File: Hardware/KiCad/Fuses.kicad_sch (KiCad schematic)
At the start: 7 parts, among them Q2 771-BUK6M61-60PX

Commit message: software pr
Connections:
- net FANS_IN: now also 12V1.2 (A), R_PD3.2
- net at Q2.4 (G), R_G3.1: no longer 12V1.2 (A), R_PD3.2
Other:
- moved on the sheet: R_G3
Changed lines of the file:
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@@
 	(wire
 		(pts
-			(xy 74.93 77.47) (xy 80.01 77.47)
+			(xy 74.93 77.47) (xy 91.44 77.47)
 		)
 		(stroke
@@
 	(wire
 		(pts
+			(xy 102.87 77.47) (xy 113.03 77.47)
+		)
+		(stroke
+			(width 0)
+			(type default)
+		)
+	)
+	(wire
+		(pts
 			(xy 102.87 59.69) (xy 102.87 64.77)
 		)
@@
 	(wire
 		(pts
-			(xy 87.63 77.47) (xy 91.44 77.47)
-		)
-		(stroke
-			(width 0)
-			(type default)
-		)
-	)
-	(wire
-		(pts
 			(xy 110.49 66.04) (xy 113.03 66.04)
 		)
@@
 	(wire
 		(pts
-			(xy 91.44 77.47) (xy 113.03 77.47)
+			(xy 91.44 77.47) (xy 95.25 77.47)
 		)
 		(stroke
@@
 	(symbol
 		(lib_id "Device:R")
-		(at 83.82 77.47 270)
+		(at 99.06 77.47 270)
 		(unit 1)
 		(exclude_from_sim no)
@@
 		(dnp no)
 		(property "Reference" "R_G3"
-			(at 81.788 75.184 90)
+			(at 97.028 75.184 90)
 			(effects
 				(font
@@
 		)
 		(property "Value" "100"
-			(at 81.788 80.01 90)
+			(at 97.028 80.01 90)
 			(effects
 				(font
@@
 		)
 		(property "Footprint" "Resistor_SMD:R_0603_1608Metric_Pad0.98x0.95mm_HandSolder"
-			(at 83.82 75.692 90)
+			(at 99.06 75.692 90)
 			(effects
 				(font
@@
 		)
 		(property "Datasheet" "~"
-			(at 83.82 77.47 0)
+			(at 99.06 77.47 0)
 			(effects
 				(font
@@
 		)
 		(property "Description" "Resistor"
-			(at 83.82 77.47 0)
+			(at 99.06 77.47 0)
 			(effects
 				(font
@@
 		)
 		(property "Manufacturer" ""
-			(at 83.82 77.47 90)
+			(at 99.06 77.47 90)
 			(effects
 				(font
@@
 		)
 		(property "Mouser Link" ""
-			(at 83.82 77.47 90)
+			(at 99.06 77.47 90)
 			(effects
 				(font
@@
 		)
 		(property "Manufacturer_Part_Number" "CRCW0603120RFKEC "
-			(at 83.82 77.47 90)
+			(at 99.06 77.47 90)
 			(effects
 				(font
@@
 		)
 		(property "Sim.Type" ""
-			(at 83.82 77.47 90)
+			(at 99.06 77.47 90)
 			(effects
 				(font
@@
 		)
 		(property "Description (Customer #)" ""
-			(at 83.82 77.47 90)
-			(effects
-				(font
+			(at 99.06 77.47 90)
+			(effects
+				(font

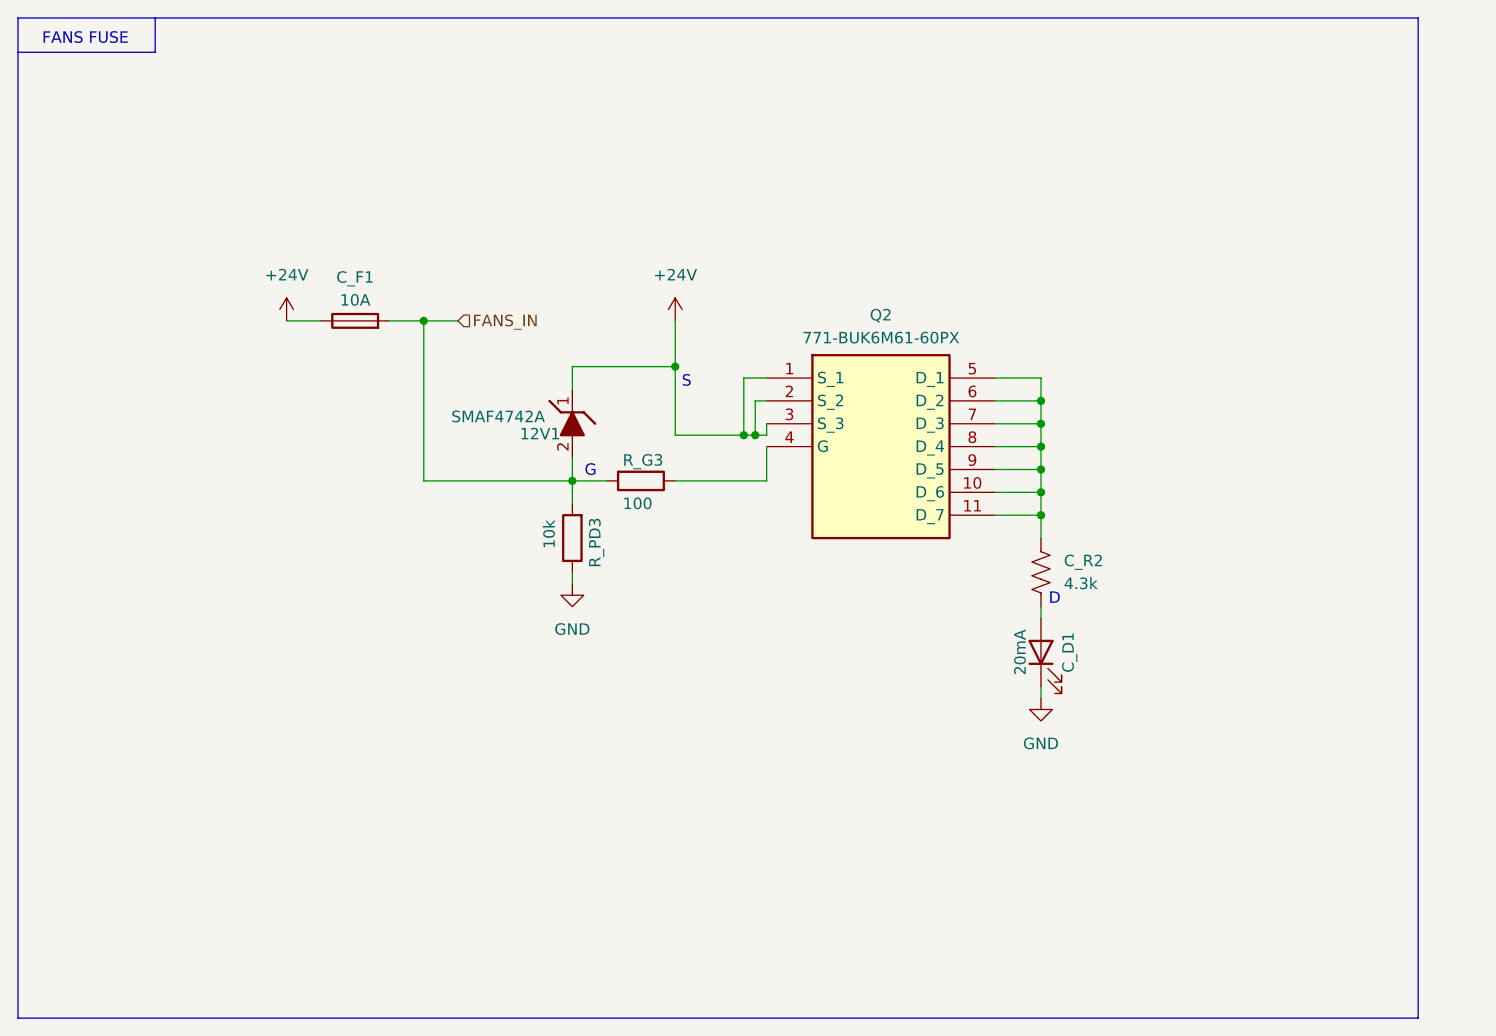
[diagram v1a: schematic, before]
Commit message: schematic changes, pre pcb revB changes
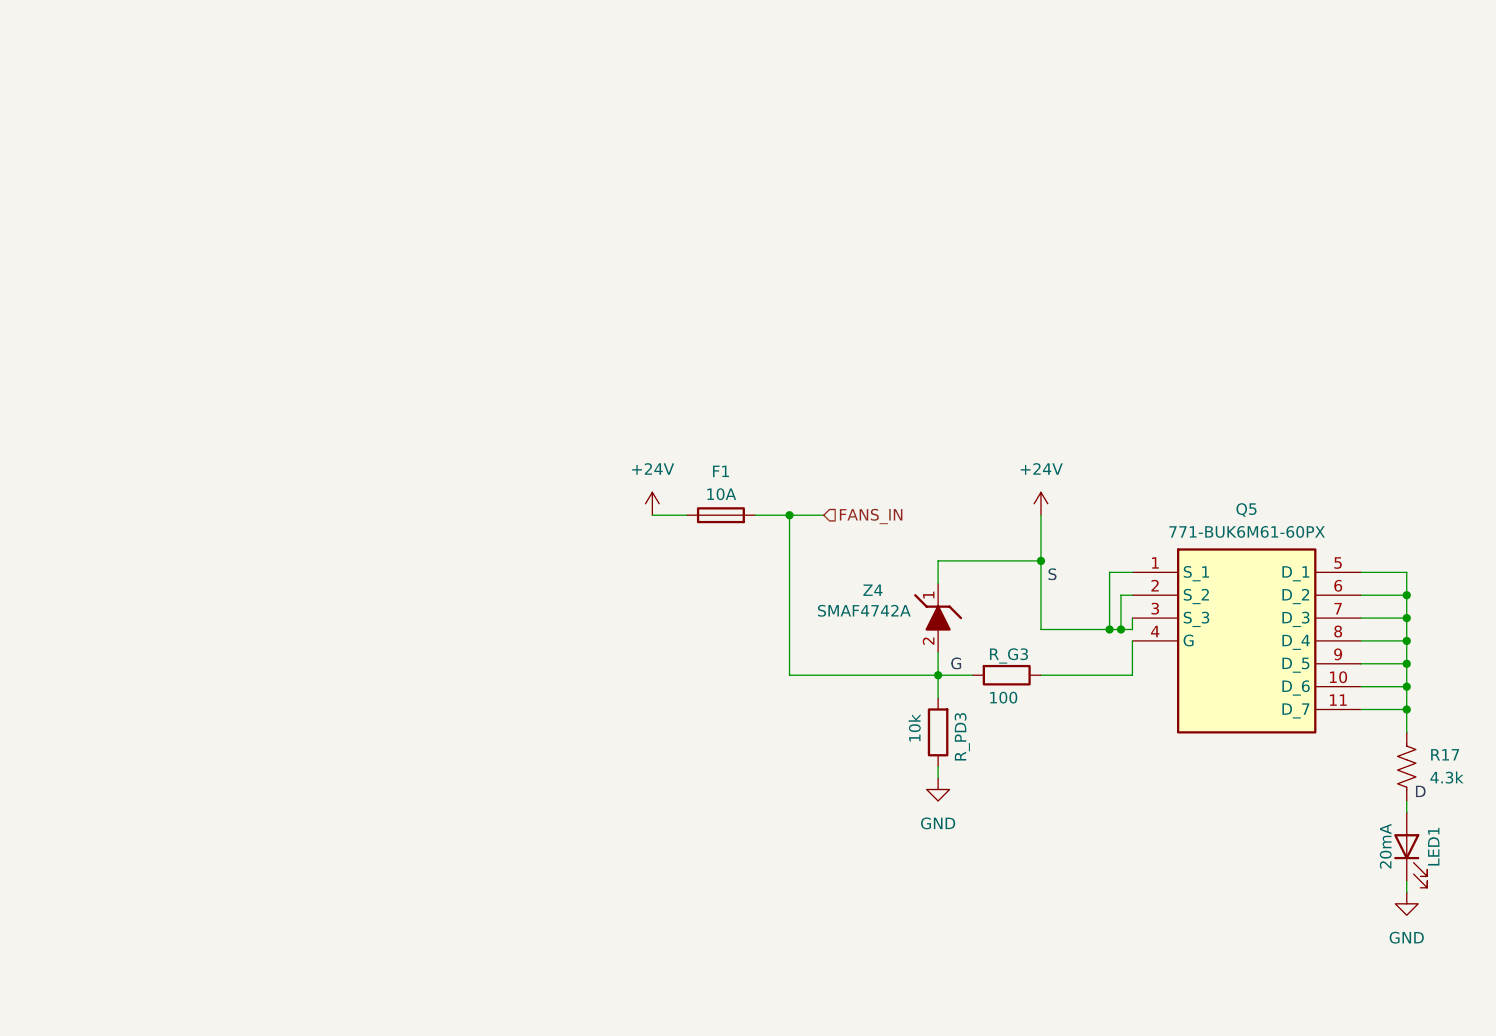
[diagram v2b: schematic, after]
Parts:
- F1: renamed from C_F1; footprint Fuse:FUSE_3568 -> Moco:FUSE_3568; LCSC (none) -> C5249699
- Q5: renamed from Q2; footprint UTSVT_Passives:BUK9M34100EX -> Moco:BUK9M34100EX
- R17: renamed from C_R2; footprint Resistor_SMD:R_0805_2012Metric -> Resistor_SMD:R_0805_2012Metric_Pad1.20x1.40mm_HandSolder
- R_PD3: LCSC (none) -> C25804
- Z4: renamed from 12V1; LCSC (none) -> C169537; Mouser Part Number 833-SMAF4749A-TP -> (none)
- renumbered C_D1 to LED1
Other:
- note removed: "FANS FUSE"
- moved on the sheet: F1, LED1, Q5, R17, R_G3, R_PD3, Z4

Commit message: sch changes, pre pcb changes
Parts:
- renumbered R17 to R15
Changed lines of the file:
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@@
 		(on_board yes)
 		(dnp no)
-		(property "Reference" "#PWR043"
+		(property "Reference" "#PWR041"
 			(at 143.51 85.09 0)
 			(effects
@@
 			(project "PS-MotorControllerInterfacePCB"
 				(path "/a2e13c19-ff3a-4e43-a7f5-200fd5b2b978/07f22498-fffc-46fc-8b11-2ac98c172822"
-					(reference "#PWR043")
+					(reference "#PWR041")
 					(unit 1)
 				)
@@
 		(dnp no)
 		(fields_autoplaced yes)
-		(property "Reference" "#PWR042"
+		(property "Reference" "#PWR040"
 			(at 132.08 116.84 0)
 			(effects
@@
 			(project "PS-MotorControllerInterfacePCB"
 				(path "/a2e13c19-ff3a-4e43-a7f5-200fd5b2b978/07f22498-fffc-46fc-8b11-2ac98c172822"
-					(reference "#PWR042")
+					(reference "#PWR040")
 					(unit 1)
 				)
@@
 		(dnp no)
 		(fields_autoplaced yes)
-		(property "Reference" "R17"
+		(property "Reference" "R15"
 			(at 186.69 107.9499 0)
 			(effects
@@
 			(project "PS-MotorControllerInterfacePCB"
 				(path "/a2e13c19-ff3a-4e43-a7f5-200fd5b2b978/07f22498-fffc-46fc-8b11-2ac98c172822"
-					(reference "R17")
+					(reference "R15")
 					(unit 1)
 				)
@@
 		(dnp no)
 		(fields_autoplaced yes)
-		(property "Reference" "#PWR044"
+		(property "Reference" "#PWR042"
 			(at 184.15 129.54 0)
 			(effects
@@
 			(project ""
 				(path "/a2e13c19-ff3a-4e43-a7f5-200fd5b2b978/07f22498-fffc-46fc-8b11-2ac98c172822"
-					(reference "#PWR044")
+					(reference "#PWR042")
 					(unit 1)
 				)
@@
 		(dnp no)
 		(fields_autoplaced yes)
-		(property "Reference" "#PWR041"
+		(property "Reference" "#PWR039"
 			(at 100.33 85.09 0)
 			(effects
@@
 			(project "PS-MotorControllerInterfacePCB"
 				(path "/a2e13c19-ff3a-4e43-a7f5-200fd5b2b978/07f22498-fffc-46fc-8b11-2ac98c172822"
-					(reference "#PWR041")
+					(reference "#PWR039")
 					(unit 1)
 				)
